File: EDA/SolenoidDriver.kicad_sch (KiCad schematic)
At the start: 8 parts, among them U8 TPS63000

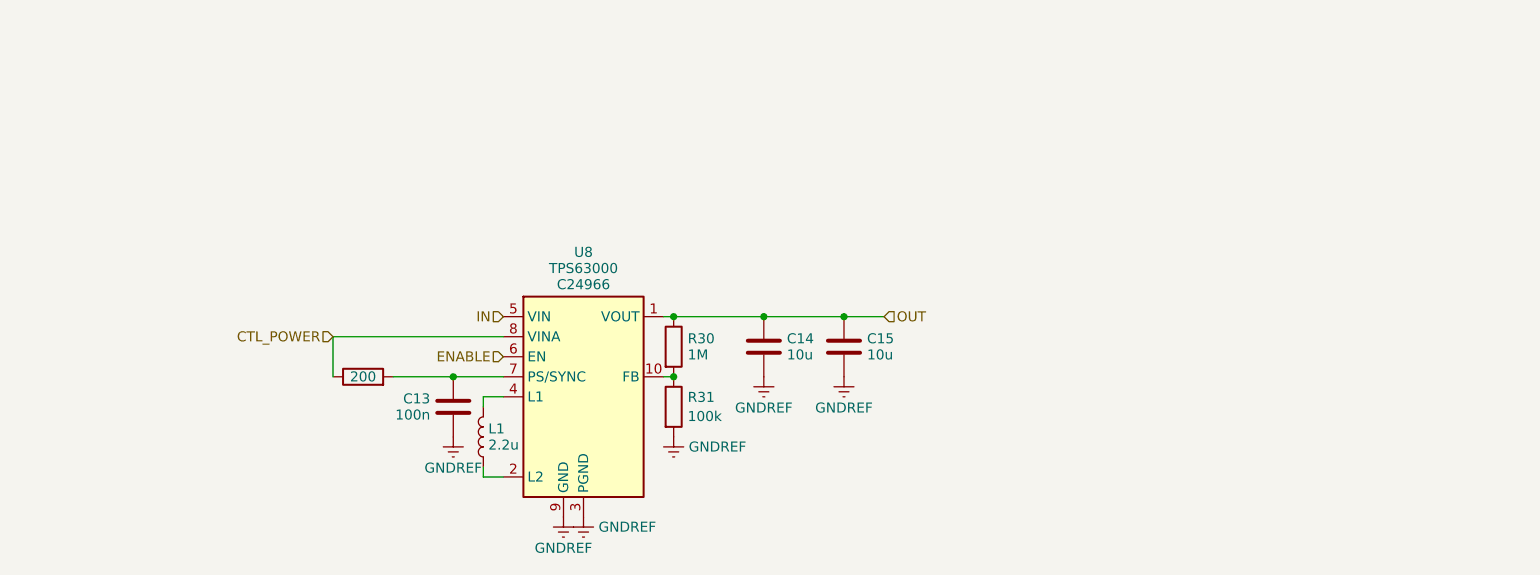
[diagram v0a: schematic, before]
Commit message: Add 12v solenoid driver
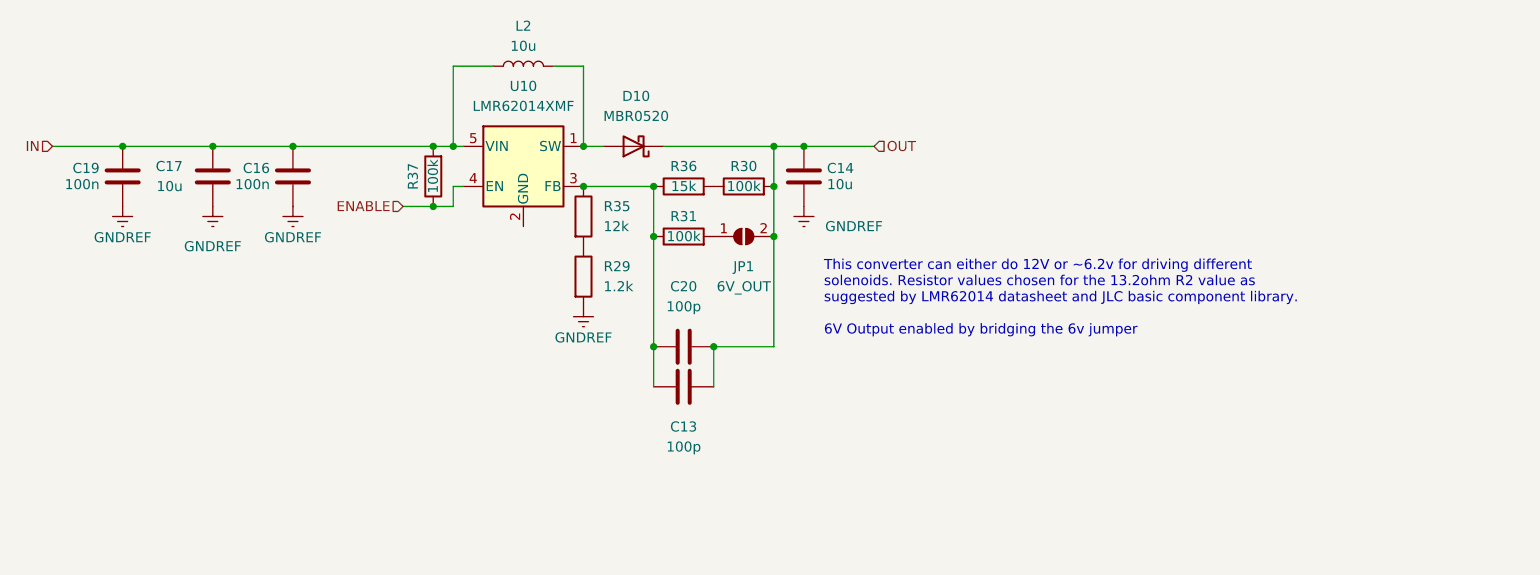
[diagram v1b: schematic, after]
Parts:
- removed C15: 10u, Capacitor_SMD:C_0603_1608Metric, symbol Library:C
- removed L1: 2.2u, Library:L_4x4, symbol Library:L
- removed U8: TPS63000, Package_SON:Texas_DRC0010J, symbol Library:TPS63001
- added C16, C19: 100n, Capacitor_SMD:C_0603_1608Metric, symbol Library:C
- added C17: 10u, Capacitor_SMD:C_0603_1608Metric, symbol Library:C
- added C20: 100p, Capacitor_SMD:C_0402_1005Metric, symbol Library:C
- added D10: MBR0520, Diode_SMD:D_SOD-123, symbol Library:MBR0520
- added JP1: 6V_OUT, symbol Jumper:SolderJumper_2_Open
- added L2: 10u, symbol Library:L
- added R35: 12k, Resistor_SMD:R_0402_1005Metric, symbol Library:R
- added R36: 15k, Resistor_SMD:R_0402_1005Metric, symbol Library:R
- added R37: 100k, Resistor_SMD:R_0402_1005Metric, symbol Library:R
- added U10: LMR62014XMF, Package_TO_SOT_SMD:SOT-23-5, symbol Regulator_Switching:LMR62014XMF
- C13: value 100n -> 100p; footprint Capacitor_SMD:C_0603_1608Metric -> Capacitor_SMD:C_0402_1005Metric; MPN C14663 -> C1546
- C14: MPN C19702 -> C96446
- R29: value 200 -> 1.2k; MPN C25087 -> C25862
- R30: value 1M -> 100k; MPN C26083 -> C25741
- R31: MPN C140218 -> C25741
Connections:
- net ENABLE: now also R37.1, U10.4 (EN)
- net GNDREF: now also R29.2, C16.1, C17.2, C19.1; no longer C13.1, R31.2
- net IN: now also C16.2, C17.1, C19.2, L2.1, R37.2, U10.5 (VIN)
- net OUT: now also C13.1, R30.2, C20.1, D10.1 (K), JP1.2 (B); no longer R30.1
- net at R31.1: now also C13.2, C20.2, R35.1, R36.1, U10.3 (FB); no longer R30.2
- net CTL_POWER: no longer names the net of R29.1
- net CTL_POWER: now also R35.2
- new net: D10.2 (A), L2.2, U10.1 (SW)
- new net: R30.1, R36.2
- new net: JP1.1 (A), R31.2
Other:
- note added: "This converter can either do 12V or ~6.2v for driving different solenoids. Resistor values chosen for the 13.2ohm R2 value as suggested by LMR62014 datasheet and JLC basic component library. 6V Output enabled by bridging the 6v jumper"

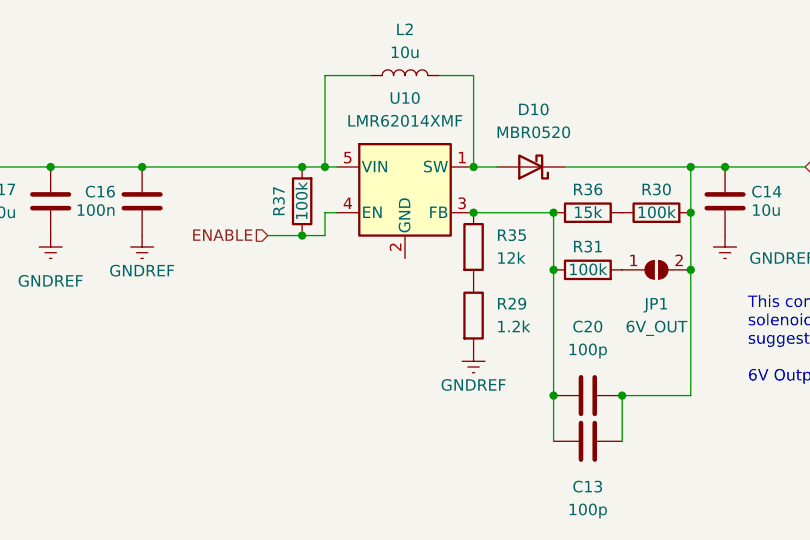
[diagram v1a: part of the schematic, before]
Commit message: Fix ERC issues
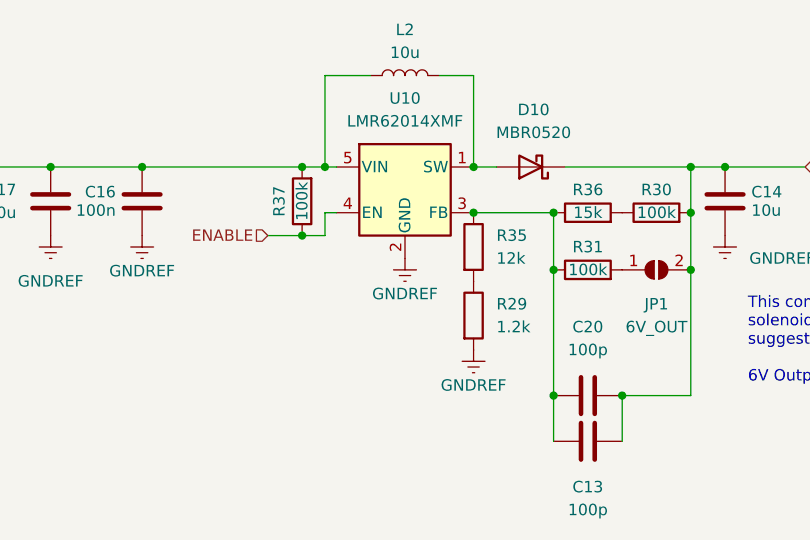
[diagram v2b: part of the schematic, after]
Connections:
- net GNDREF: now also U10.2 (GND)
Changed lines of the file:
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@@
+    )
+  )
+  (symbol (lib_id "power:GNDREF") (at 143.51 77.47 0) (unit 1)
+    (in_bom yes) (on_board yes) (dnp no) (fields_autoplaced)
+    (property "Reference" "#PWR011" (at 143.51 83.82 0)
+      (effects (font (size 1.27 1.27)) hide)
+    )
+    (property "Value" "GNDREF" (at 143.51 81.415 0)
+      (effects (font (size 1.27 1.27)))
+    )
+    (property "Footprint" "" (at 143.51 77.47 0)
+      (effects (font (size 1.27 1.27)) hide)
+    )
+    (property "Datasheet" "" (at 143.51 77.47 0)
+      (effects (font (size 1.27 1.27)) hide)
+    )
+    (pin "1")
+    (instances
+      (project "DiveCAN Head2"
+        (path "/ab021047-3849-453b-b3dc-d234ace3779d/9021e904-ec93-4c28-9903-7bba14359351"
+          (reference "#PWR011") (unit 1)
+        )
+      )
     )
   )

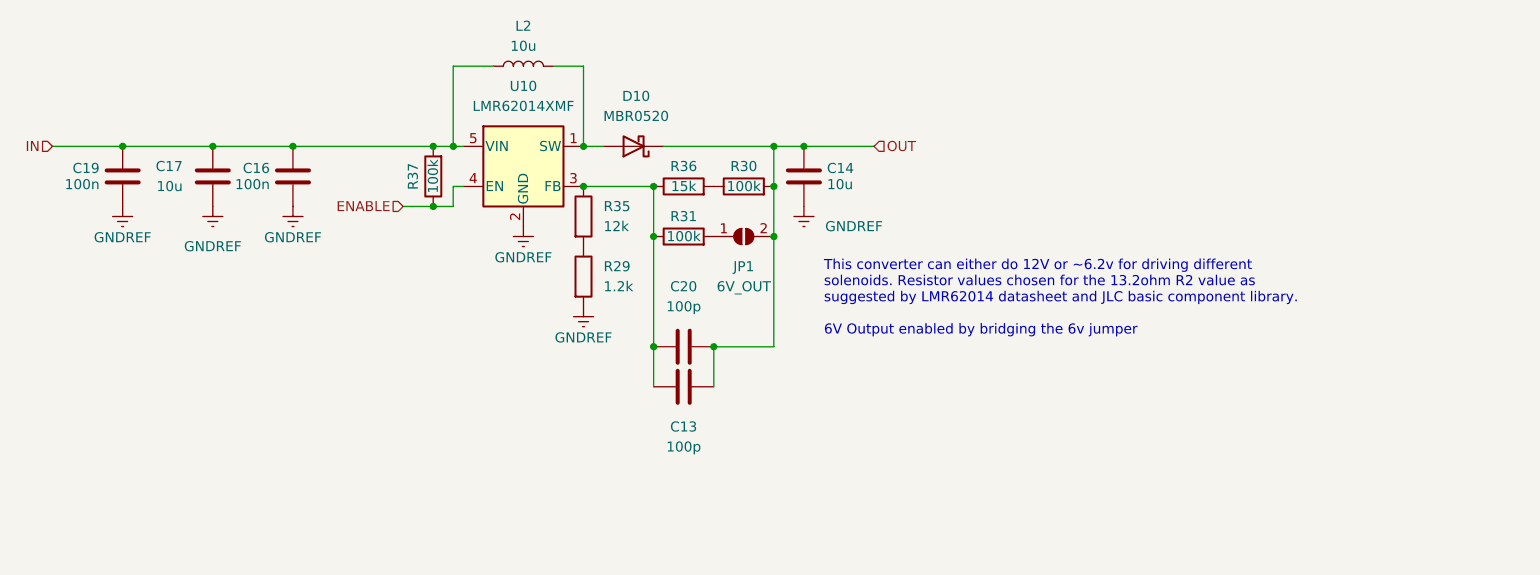
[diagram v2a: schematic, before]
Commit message: Renumber schematic
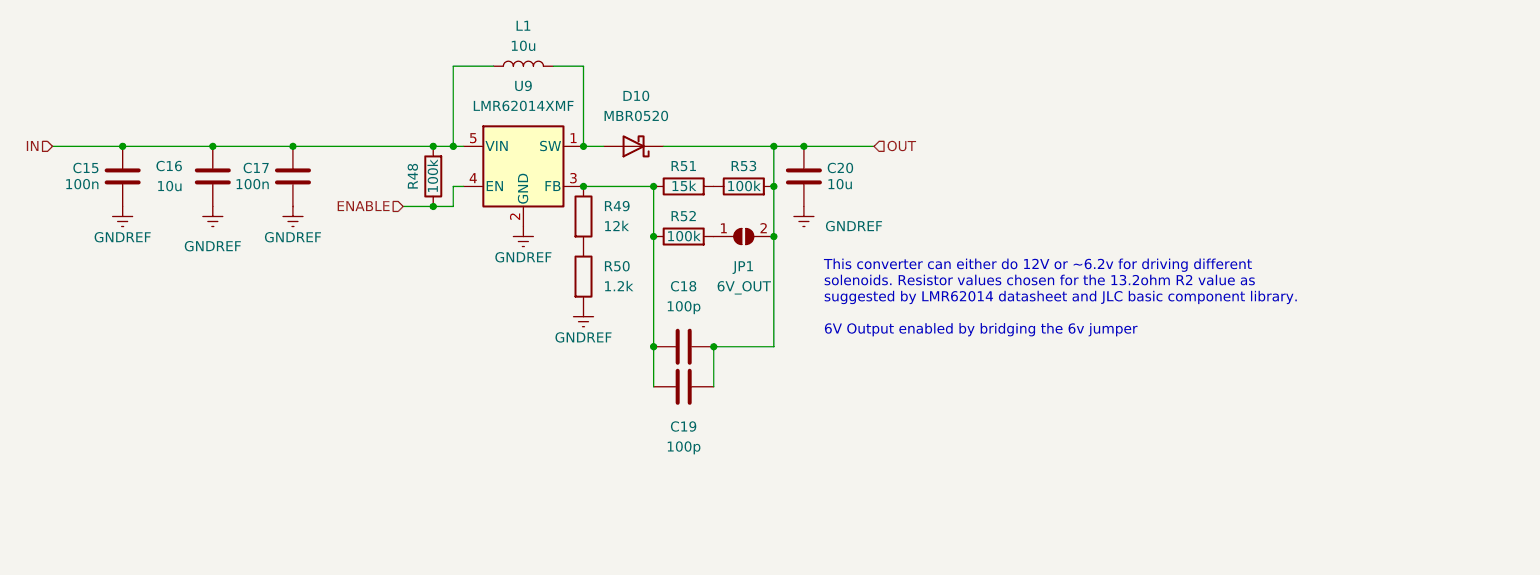
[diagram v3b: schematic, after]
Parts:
- renumbered C19 to C15, C17 to C16, C16 to C17, C20 to C18, C13 to C19, C14 to C20, L2 to L1, R37 to R48, R35 to R49, R29 to R50, R36 to R51, R31 to R52, R30 to R53, U10 to U9
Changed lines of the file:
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@@
   (symbol (lib_id "Library:R") (at 163.83 72.39 90) (unit 1)
     (in_bom yes) (on_board yes) (dnp no)
-    (property "Reference" "R36" (at 163.83 69.85 90)
+    (property "Reference" "R51" (at 163.83 69.85 90)
       (effects (font (size 1.27 1.27)))
     )
@@
       (project "DiveCAN Head2"
         (path "/ab021047-3849-453b-b3dc-d234ace3779d/9021e904-ec93-4c28-9903-7bba14359351"
-          (reference "R36") (unit 1)
+          (reference "R51") (unit 1)
         )
       )
@@
   (symbol (lib_id "Library:R") (at 151.13 76.2 0) (unit 1)
     (in_bom yes) (on_board yes) (dnp no) (fields_autoplaced)
-    (property "Reference" "R35" (at 153.67 74.93 0)
+    (property "Reference" "R49" (at 153.67 74.93 0)
       (effects (font (size 1.27 1.27)) (justify left))
     )
@@
       (project "DiveCAN Head2"
         (path "/ab021047-3849-453b-b3dc-d234ace3779d/9021e904-ec93-4c28-9903-7bba14359351"
-          (reference "R35") (unit 1)
+          (reference "R49") (unit 1)
         )
       )
@@
   (symbol (lib_id "Library:R") (at 132.08 71.12 180) (unit 1)
     (in_bom yes) (on_board yes) (dnp no)
-    (property "Reference" "R37" (at 129.54 71.12 90)
+    (property "Reference" "R48" (at 129.54 71.12 90)
       (effects (font (size 1.27 1.27)))
     )
@@
       (project "DiveCAN Head2"
         (path "/ab021047-3849-453b-b3dc-d234ace3779d/9021e904-ec93-4c28-9903-7bba14359351"
-          (reference "R37") (unit 1)
+          (reference "R48") (unit 1)
         )
       )
@@
   (symbol (lib_id "power:GNDREF") (at 151.13 87.63 0) (unit 1)
     (in_bom yes) (on_board yes) (dnp no) (fields_autoplaced)
-    (property "Reference" "#PWR048" (at 151.13 93.98 0)
+    (property "Reference" "#PWR064" (at 151.13 93.98 0)
       (effects (font (size 1.27 1.27)) hide)
     )
@@
       (project "DiveCAN Head2"
         (path "/ab021047-3849-453b-b3dc-d234ace3779d/9021e904-ec93-4c28-9903-7bba14359351"
-          (reference "#PWR048") (unit 1)
+          (reference "#PWR064") (unit 1)
         )
       )
@@
   (symbol (lib_id "Regulator_Switching:LMR62014XMF") (at 143.51 69.85 0) (unit 1)
     (in_bom yes) (on_board yes) (dnp no) (fields_autoplaced)
-    (property "Reference" "U10" (at 143.51 59.69 0)
+    (property "Reference" "U9" (at 143.51 59.69 0)
       (effects (font (size 1.27 1.27)))
     )
@@
       (project "DiveCAN Head2"
         (path "/ab021047-3849-453b-b3dc-d234ace3779d/9021e904-ec93-4c28-9903-7bba14359351"
-          (reference "U10") (unit 1)
+          (reference "U9") (unit 1)
         )
       )
@@
   (symbol (lib_id "Library:C") (at 114.3 71.12 180) (unit 1)
     (in_bom yes) (on_board yes) (dnp no) (fields_autoplaced)
-    (property "Reference" "C16" (at 111.3791 70.096 0)
+    (property "Reference" "C17" (at 111.3791 70.096 0)
       (effects (font (size 1.27 1.27)) (justify left))
     )
@@
       (project "DiveCAN Head2"
         (path "/ab021047-3849-453b-b3dc-d234ace3779d/9021e904-ec93-4c28-9903-7bba14359351"
-          (reference "C16") (unit 1)
+          (reference "C17") (unit 1)
         )
       )
@@
   (symbol (lib_id "power:GNDREF") (at 114.3 74.93 0) (unit 1)
     (in_bom yes) (on_board yes) (dnp no) (fields_autoplaced)
-    (property "Reference" "#PWR056" (at 114.3 81.28 0)
+    (property "Reference" "#PWR062" (at 114.3 81.28 0)
       (effects (font (size 1.27 1.27)) hide)
     )
@@
       (project "DiveCAN Head2"
         (path "/ab021047-3849-453b-b3dc-d234ace3779d/9021e904-ec93-4c28-9903-7bba14359351"
-          (reference "#PWR056") (unit 1)
+          (reference "#PWR062") (unit 1)
         )
       )
@@
   (symbol (lib_id "Library:R") (at 163.83 78.74 90) (unit 1)
     (in_bom yes) (on_board yes) (dnp no)
-    (property "Reference" "R31" (at 163.83 76.2 90)
+    (property "Reference" "R52" (at 163.83 76.2 90)
       (effects (font (size 1.27 1.27)))
     )
@@
       (project "DiveCAN Head2"
         (path "/ab021047-3849-453b-b3dc-d234ace3779d/9021e904-ec93-4c28-9903-7bba14359351"
-          (reference "R31") (unit 1)
+          (reference "R52") (unit 1)
         )
       )
@@
   (symbol (lib_id "Library:C") (at 104.14 71.12 0) (unit 1)
     (in_bom yes) (on_board yes) (dnp no) (fields_autoplaced)
-    (property "Reference" "C17" (at 100.33 69.85 0)
+    (property "Reference" "C16" (at 100.33 69.85 0)
       (effects (font (size 1.27 1.27)) (justify right))
     )
@@
       (project "DiveCAN Head2"
         (path "/ab021047-3849-453b-b3dc-d234ace3779d/9021e904-ec93-4c28-9903-7bba14359351"
-          (reference "C17") (unit 1)
+          (reference "C16") (unit 1)
         )
       )
@@
   (symbol (lib_id "power:GNDREF") (at 179.07 74.93 0) (unit 1)
     (in_bom yes) (on_board yes) (dnp no)
-    (property "Reference" "#PWR052" (at 179.07 81.28 0)
+    (property "Reference" "#PWR065" (at 179.07 81.28 0)
       (effects (font (size 1.27 1.27)) hide)
     )
@@
       (project "DiveCAN Head2"
         (path "/ab021047-3849-453b-b3dc-d234ace3779d/9021e904-ec93-4c28-9903-7bba14359351"
-          (reference "#PWR052") (unit 1)
+          (reference "#PWR065") (unit 1)
         )
       )
@@
   (symbol (lib_id "Library:C") (at 163.83 97.79 270) (unit 1)
     (in_bom yes) (on_board yes) (dnp no) (fields_autoplaced)
-    (property "Reference" "C13" (at 163.83 102.87 90)
+    (property "Reference" "C19" (at 163.83 102.87 90)
       (effects (font (size 1.27 1.27)))
     )
@@
       (project "DiveCAN Head2"
         (path "/ab021047-3849-453b-b3dc-d234ace3779d/9021e904-ec93-4c28-9903-7bba14359351"
-          (reference "C13") (unit 1)
+          (reference "C19") (unit 1)
         )
       )
@@
   (symbol (lib_id "Library:C") (at 163.83 92.71 270) (unit 1)
     (in_bom yes) (on_board yes) (dnp no) (fields_autoplaced)
-    (property "Reference" "C20" (at 163.83 85.09 90)
+    (property "Reference" "C18" (at 163.83 85.09 90)
       (effects (font (size 1.27 1.27)))
     )
@@
       (project "DiveCAN Head2"
         (path "/ab021047-3849-453b-b3dc-d234ace3779d/9021e904-ec93-4c28-9903-7bba14359351"
-          (reference "C20") (unit 1)
+          (reference "C18") (unit 1)
         )
       )
@@
   (symbol (lib_id "power:GNDREF") (at 143.51 77.47 0) (unit 1)
     (in_bom yes) (on_board yes) (dnp no) (fields_autoplaced)
-    (property "Reference" "#PWR011" (at 143.51 83.82 0)
+    (property "Reference" "#PWR063" (at 143.51 83.82 0)
       (effects (font (size 1.27 1.27)) hide)
     )
@@
       (project "DiveCAN Head2"
         (path "/ab021047-3849-453b-b3dc-d234ace3779d/9021e904-ec93-4c28-9903-7bba14359351"
-          (reference "#PWR011") (unit 1)
+          (reference "#PWR063") (unit 1)
         )
       )
@@
   (symbol (lib_id "Library:R") (at 151.13 83.82 0) (unit 1)
     (in_bom yes) (on_board yes) (dnp no) (fields_autoplaced)
-    (property "Reference" "R29" (at 153.67 82.55 0)
+    (property "Reference" "R50" (at 153.67 82.55 0)
       (effects (font (size 1.27 1.27)) (justify left))
     )
@@
       (project "DiveCAN Head2"
         (path "/ab021047-3849-453b-b3dc-d234ace3779d/9021e904-ec93-4c28-9903-7bba14359351"
-          (reference "R29") (unit 1)
+          (reference "R50") (unit 1)
         )
       )
@@
   (symbol (lib_id "Library:R") (at 171.45 72.39 90) (unit 1)
     (in_bom yes) (on_board yes) (dnp no)
-    (property "Reference" "R30" (at 171.45 69.85 90)
+    (property "Reference" "R53" (at 171.45 69.85 90)
       (effects (font (size 1.27 1.27)))
     )
@@
       (project "DiveCAN Head2"
         (path "/ab021047-3849-453b-b3dc-d234ace3779d/9021e904-ec93-4c28-9903-7bba14359351"
-          (reference "R30") (unit 1)
+          (reference "R53") (unit 1)
         )
       )
@@
   (symbol (lib_id "Library:C") (at 179.07 71.12 0) (unit 1)
     (in_bom yes) (on_board yes) (dnp no) (fields_autoplaced)
-    (property "Reference" "C14" (at 181.991 70.096 0)
+    (property "Reference" "C20" (at 181.991 70.096 0)
       (effects (font (size 1.27 1.27)) (justify left))
     )
@@
       (project "DiveCAN Head2"
         (path "/ab021047-3849-453b-b3dc-d234ace3779d/9021e904-ec93-4c28-9903-7bba14359351"
-          (reference "C14") (unit 1)
+          (reference "C20") (unit 1)
         )
       )
@@
   (symbol (lib_id "power:GNDREF") (at 104.14 74.93 0) (unit 1)
     (in_bom yes) (on_board yes) (dnp no) (fields_autoplaced)
-    (property "Reference" "#PWR057" (at 104.14 81.28 0)
+    (property "Reference" "#PWR061" (at 104.14 81.28 0)
       (effects (font (size 1.27 1.27)) hide)
     )
@@
       (project "DiveCAN Head2"
         (path "/ab021047-3849-453b-b3dc-d234ace3779d/9021e904-ec93-4c28-9903-7bba14359351"
-          (reference "#PWR057") (unit 1)
+          (reference "#PWR061") (unit 1)
         )
       )
@@
   (symbol (lib_id "Library:C") (at 92.71 71.12 180) (unit 1)
     (in_bom yes) (on_board yes) (dnp no) (fields_autoplaced)
-    (property "Reference" "C19" (at 89.7891 70.096 0)
+    (property "Reference" "C15" (at 89.7891 70.096 0)
       (effects (font (size 1.27 1.27)) (justify left))
     )
@@
       (project "DiveCAN Head2"
         (path "/ab021047-3849-453b-b3dc-d234ace3779d/9021e904-ec93-4c28-9903-7bba14359351"
-          (reference "C19") (unit 1)
+          (reference "C15") (unit 1)
         )
       )
@@
   (symbol (lib_id "Library:L") (at 143.51 57.15 90) (unit 1)
     (in_bom yes) (on_board yes) (dnp no) (fields_autoplaced)
-    (property "Reference" "L2" (at 143.51 52.07 90)
+    (property "Reference" "L1" (at 143.51 52.07 90)
       (effects (font (size 1.27 1.27)))
     )
@@
       (project "DiveCAN Head2"
         (path "/ab021047-3849-453b-b3dc-d234ace3779d/9021e904-ec93-4c28-9903-7bba14359351"
-          (reference "L2") (unit 1)
-        )
-      )
+          (reference "L1") (unit 1)
+        )
+      )
